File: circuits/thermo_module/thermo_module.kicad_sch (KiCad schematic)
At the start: 14 parts, among them IC3 LM285Z-1.2, IC4 TMP36

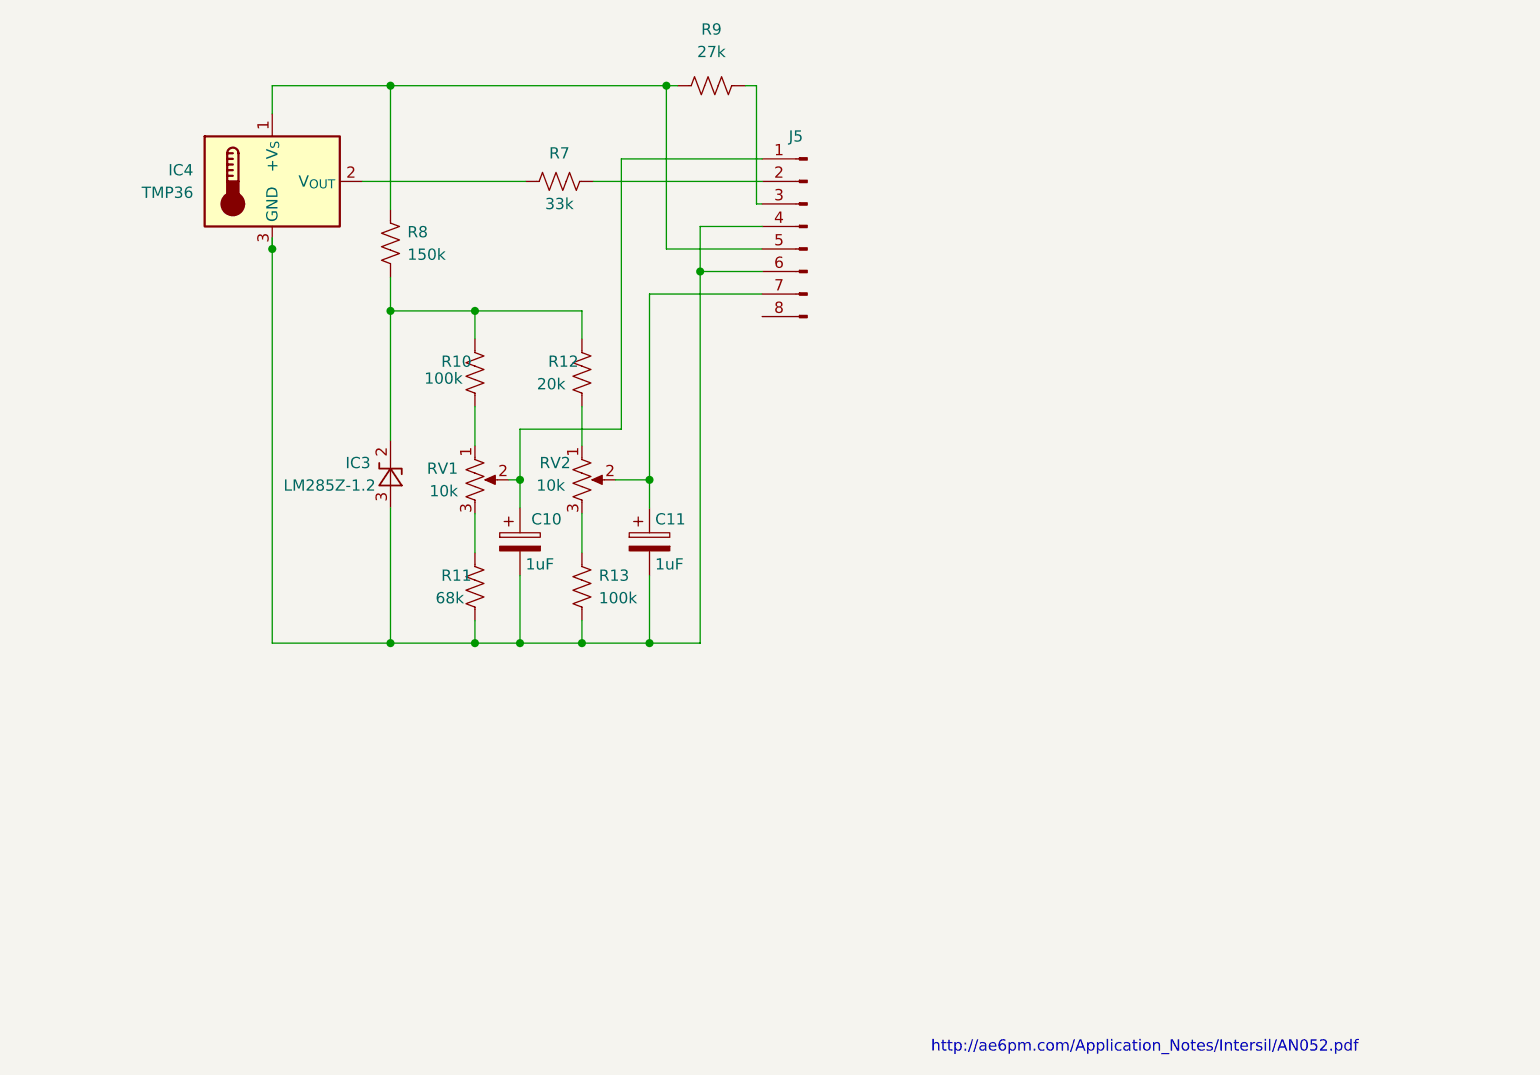
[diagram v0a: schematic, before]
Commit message: Redesign thermo module to make it work
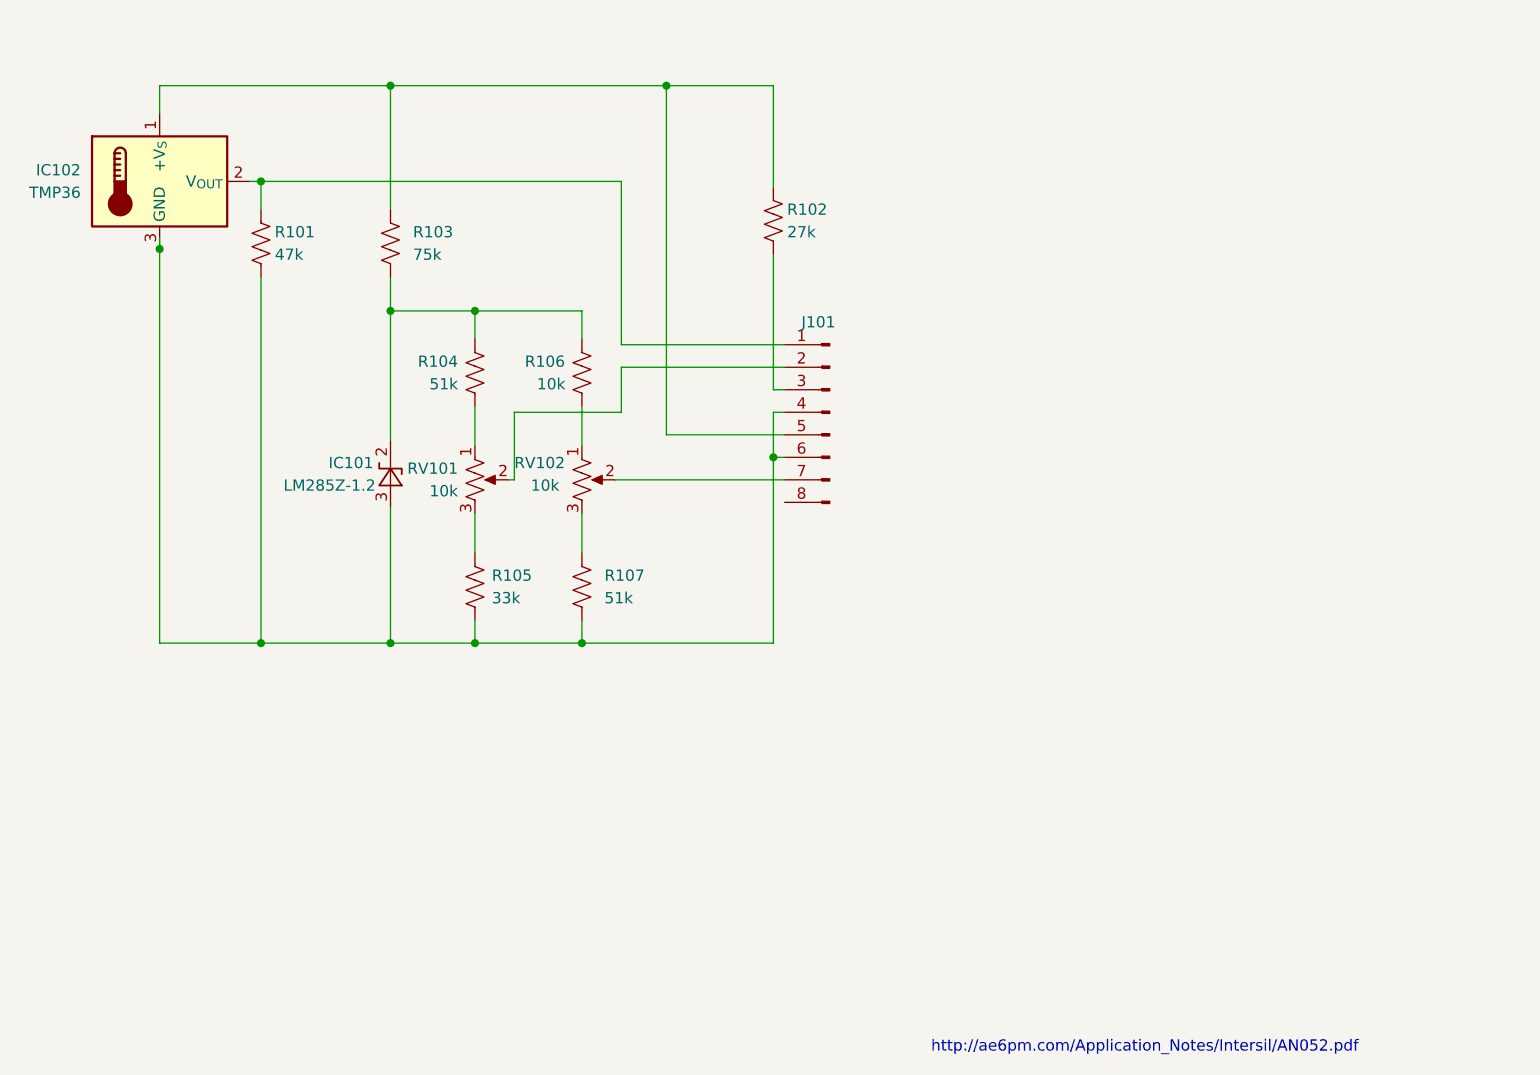
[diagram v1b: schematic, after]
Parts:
- removed C10, C11: 1uF, Capacitor_THT:CP_Radial_D5.0mm_P2.50mm, symbol Device:C_Polarized
- removed J5: ~, Connector_PinHeader_2.54mm:PinHeader_1x08_P2.54mm_Vertical, symbol Connector:Conn_01x08_Pin
- removed R7: 33k, Resistor_THT:R_Axial_DIN0204_L3.6mm_D1.6mm_P7.62mm_Horizontal, symbol Device:R_US
- added J101: ~, Connector_PinHeader_2.54mm:PinHeader_1x08_P2.54mm_Vertical, symbol Connector:Conn_01x08_Pin
- added R101: 47k, Resistor_THT:R_Axial_DIN0204_L3.6mm_D1.6mm_P7.62mm_Horizontal, symbol Device:R_US
- R103: renamed from R8; value 150k -> 75k
- R104: renamed from R10; value 100k -> 51k
- R105: renamed from R11; value 68k -> 33k
- R106: renamed from R12; value 20k -> 10k
- R107: renamed from R13; value 100k -> 51k
- renumbered IC3 to IC101, IC4 to IC102, R9 to R102, RV1 to RV101, RV2 to RV102
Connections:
- net at RV101.2: now also J101.2 (Pin_2)
- net at R102.2: now also J101.3 (Pin_3)
- net at IC101.3 (A), IC102.3 (GND), R105.2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: now also J101.4 (Pin_4), J101.6 (Pin_6), R101.1
- net at IC102.1 (+V_{S}), R102.1, R103.1: now also J101.5 (Pin_5)
- net at RV102.2: now also J101.7 (Pin_7)
- net at IC102.2 (V_{OUT}): now also J101.1 (Pin_1), R101.2
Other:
- moved on the sheet: IC102, R102

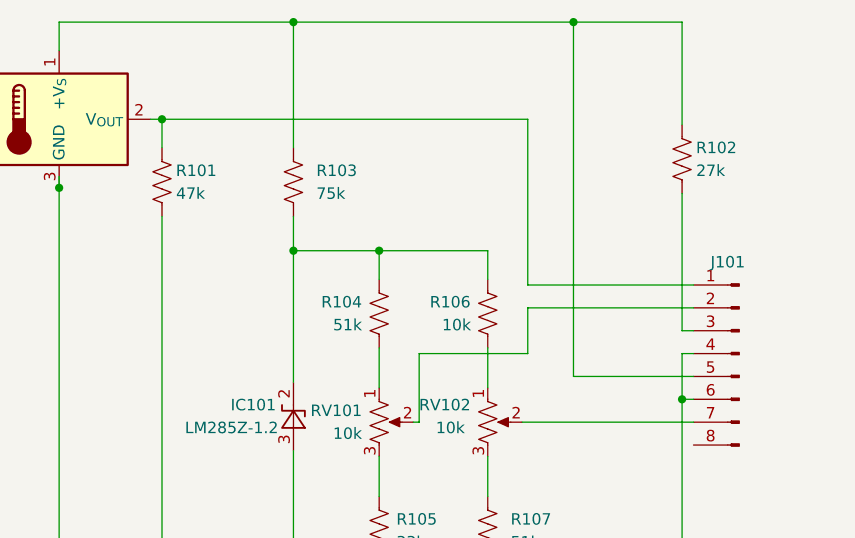
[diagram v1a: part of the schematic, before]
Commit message: Fix for input pins the wrong way round
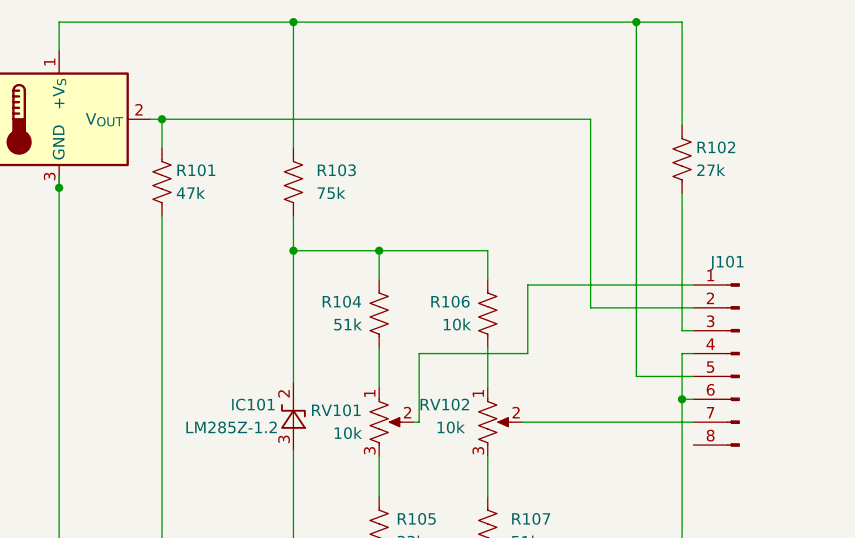
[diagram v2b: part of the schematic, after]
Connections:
- net at IC102.2 (V_{OUT}), R101.2: now also J101.2 (Pin_2); no longer J101.1 (Pin_1)
- net at RV101.2: now also J101.1 (Pin_1); no longer J101.2 (Pin_2)
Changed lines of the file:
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@@
   (junction (at 92.075 80.01) (diameter 0) (color 0 0 0 0)
   )
-  (junction (at 149.225 61.595) (diameter 0) (color 0 0 0 0)
+  (junction (at 161.29 103.505) (diameter 0) (color 0 0 0 0)
   )
-  (junction (at 161.29 103.505) (diameter 0) (color 0 0 0 0)
+  (junction (at 156.21 61.595) (diameter 0) (color 0 0 0 0)
   )
   (junction (at 127.635 86.995) (diameter 0) (color 0 0 0 0)
@@
   (junction (at 118.11 86.995) (diameter 0) (color 0 0 0 0)
   )
-  (wire (pts (xy 149.225 100.965) (xy 162.56 100.965))
+  (wire (pts (xy 156.21 100.965) (xy 162.56 100.965))
     (stroke (width 0) (type default))
   )
@@
     (stroke (width 0) (type default))
   )
-  (wire (pts (xy 118.11 61.595) (xy 149.225 61.595))
+  (wire (pts (xy 118.11 61.595) (xy 156.21 61.595))
     (stroke (width 0) (type default))
   )
@@
     (stroke (width 0) (type default))
   )
-  (wire (pts (xy 149.225 61.595) (xy 149.225 100.965))
-    (stroke (width 0) (type default))
-  )
-  (wire (pts (xy 144.145 90.805) (xy 162.56 90.805))
+  (wire (pts (xy 156.21 61.595) (xy 156.21 100.965))
     (stroke (width 0) (type default))
   )
@@
     (stroke (width 0) (type default))
   )
-  (wire (pts (xy 103.505 72.39) (xy 144.145 72.39))
+  (wire (pts (xy 103.505 72.39) (xy 151.13 72.39))
     (stroke (width 0) (type default))
   )
@@
     (stroke (width 0) (type default))
   )
-  (wire (pts (xy 144.145 93.345) (xy 144.145 98.425))
+  (wire (pts (xy 144.145 90.805) (xy 162.56 90.805))
+    (stroke (width 0) (type default))
+  )
+  (wire (pts (xy 144.145 90.805) (xy 144.145 98.425))
     (stroke (width 0) (type default))
   )
@@
     (stroke (width 0) (type default))
   )
+  (wire (pts (xy 156.21 61.595) (xy 161.29 61.595))
+    (stroke (width 0) (type default))
+  )
   (wire (pts (xy 118.11 124.46) (xy 127.635 124.46))
     (stroke (width 0) (type default))
@@
     (stroke (width 0) (type default))
   )
-  (wire (pts (xy 162.56 93.345) (xy 144.145 93.345))
+  (wire (pts (xy 151.13 93.345) (xy 162.56 93.345))
     (stroke (width 0) (type default))
   )
@@
   )
   (wire (pts (xy 132.08 106.045) (xy 131.445 106.045))
-    (stroke (width 0) (type default))
-  )
-  (wire (pts (xy 149.225 61.595) (xy 161.29 61.595))
     (stroke (width 0) (type default))
   )
@@
     (stroke (width 0) (type default))
   )
-  (wire (pts (xy 144.145 72.39) (xy 144.145 90.805))
+  (wire (pts (xy 151.13 72.39) (xy 151.13 93.345))
     (stroke (width 0) (type default))
   )
